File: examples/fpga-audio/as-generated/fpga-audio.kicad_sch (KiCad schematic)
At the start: 29 parts, among them J1 3V3 IN, J2 AUDIO OUT, J3 SPI PROG, U1 iCE40UP5K, U2 PCM5102A, U3 AP2112K-1.2, U4 W25Q32JV, X1 12MHz

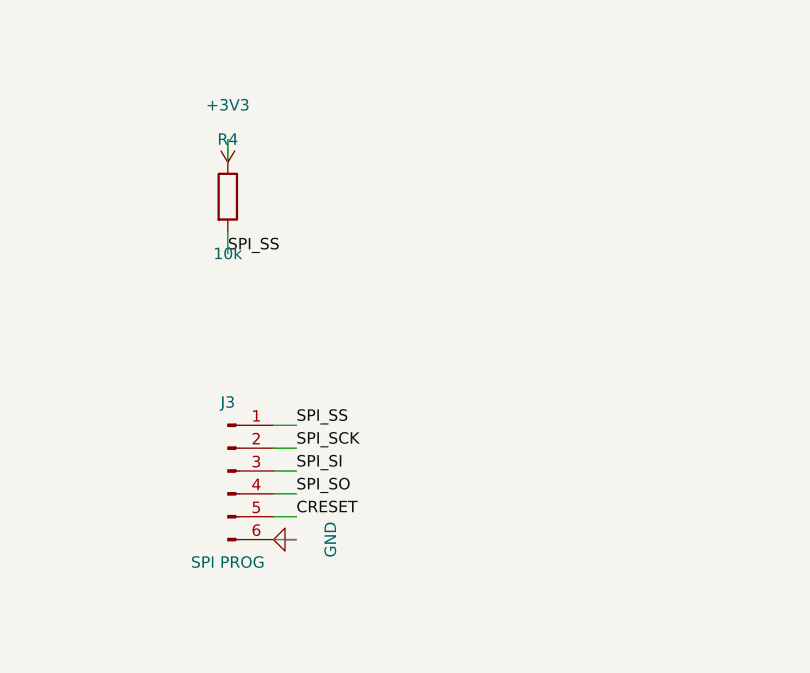
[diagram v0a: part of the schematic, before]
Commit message: Route the sheets, and anchor the ground vias where the loop is
The user's verdict on the last round stood: none of the five schematics
read as a human drawing, and the artwork still had its physics wrong.
This round answers both.

The schematic side replaces the stub-and-label sheet with a router.
Every signal net becomes a tree of straight, L-, Z- and detour-shaped
runs on the 1.27 mm grid: legs leave a pin along its own stub, escape
distances stagger so a bus does not fight over one column, every pin
reserves a runway another wire may cross but not ride along, and the
sheet frame, title block and notes are obstacles like any symbol.
Fragments merge Kruskal-style so a rail whose regulator is boxed in
still gets its capacitors chained; each surviving fragment keeps one
label, because the label is what names the net. Collinear same-net
segments are unioned and then split at every tee - KiCad 9's
connectivity requires files drawn the way the editor draws them, with
a junction dot and a wire break wherever a branch tees in, and a wire
that runs through a junction connects on one side of it only. That
last fact cost an evening and is now a comment.

Trying to draw the wires found what no rule had: the buck's LED was
upside down with its ground pointing up into the resistor above it,
both breakout headers faced away from everything they connect to
(fixed with mirrored symbols, which Part now supports), the FPGA
sheet's notes printed over the 1.2 V regulator, and its programming
header sat inside the title block. Wired: buck, motor and op-amp
completely; the Pico carrier 31 of 33 nets; the FPGA board 16 of 19 -
what stays labelled is what a human would label too.

The artwork side anchors every FPGA decoupling capacitor's ground via
against its own pad, on the far side from the supply pad, with the
1.2 mm stub as the whole loop - retiring all seven
layout.decoupling_via findings and that waiver with them. A back_cost
experiment (0.4 to 0.6) to shrink the return-path cuts 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
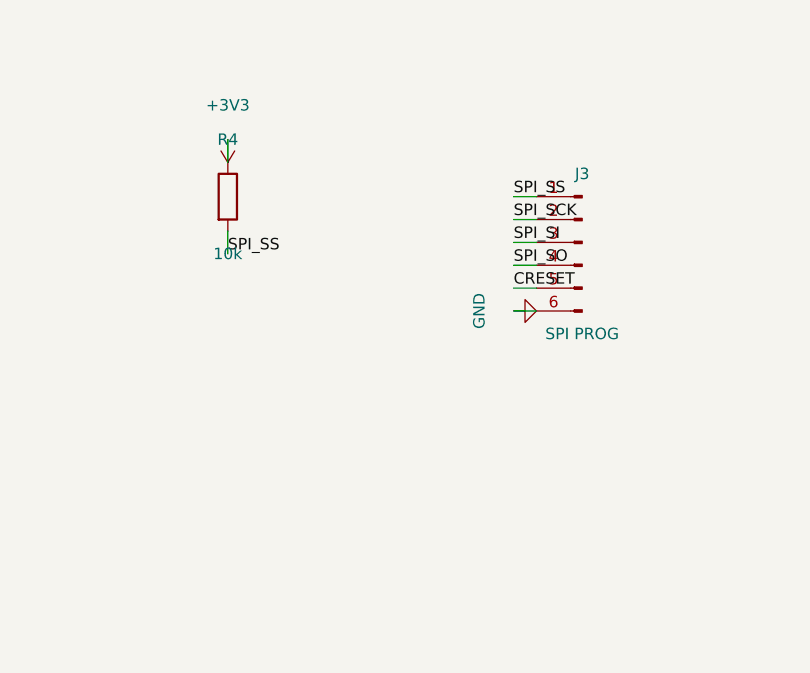
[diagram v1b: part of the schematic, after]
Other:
- moved on the sheet: J3
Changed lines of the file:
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@@
     (instances (project "fpga-audio" (path "/434dea94-d96f-5288-b60c-67317d440f4e" (reference "J2") (unit 1))))
   )
-  (wire (pts (xy 335.59 265.24) (xy 338.13 265.24)) (stroke (width 0) (type default)))
-  (label "SPI_SS" (at 338.13 265.24 0) (effects (font (size 1.27 1.27)) (justify left bottom)))
-  (wire (pts (xy 335.59 267.78) (xy 338.13 267.78)) (stroke (width 0) (type default)))
-  (label "SPI_SCK" (at 338.13 267.78 0) (effects (font (size 1.27 1.27)) (justify left bottom)))
-  (wire (pts (xy 335.59 270.32) (xy 338.13 270.32)) (stroke (width 0) (type default)))
-  (label "SPI_SI" (at 338.13 270.32 0) (effects (font (size 1.27 1.27)) (justify left bottom)))
-  (wire (pts (xy 335.59 272.86) (xy 338.13 272.86)) (stroke (width 0) (type default)))
-  (label "SPI_SO" (at 338.13 272.86 0) (effects (font (size 1.27 1.27)) (justify left bottom)))
-  (wire (pts (xy 335.59 275.4) (xy 338.13 275.4)) (stroke (width 0) (type default)))
-  (label "CRESET" (at 338.13 275.4 0) (effects (font (size 1.27 1.27)) (justify left bottom)))
-  (wire (pts (xy 335.59 277.94) (xy 338.13 277.94)) (stroke (width 0) (type default)))
-  (symbol (lib_id "power:GND") (at 338.13 277.94 270) (unit 1)
+  (wire (pts (xy 364.8 239.84) (xy 362.26 239.84)) (stroke (width 0) (type default)))
+  (label "SPI_SS" (at 362.26 239.84 0) (effects (font (size 1.27 1.27)) (justify left bottom)))
+  (wire (pts (xy 364.8 242.38) (xy 362.26 242.38)) (stroke (width 0) (type default)))
+  (label "SPI_SCK" (at 362.26 242.38 0) (effects (font (size 1.27 1.27)) (justify left bottom)))
+  (wire (pts (xy 364.8 244.92) (xy 362.26 244.92)) (stroke (width 0) (type default)))
+  (label "SPI_SI" (at 362.26 244.92 0) (effects (font (size 1.27 1.27)) (justify left bottom)))
+  (wire (pts (xy 364.8 247.46) (xy 362.26 247.46)) (stroke (width 0) (type default)))
+  (label "SPI_SO" (at 362.26 247.46 0) (effects (font (size 1.27 1.27)) (justify left bottom)))
+  (wire (pts (xy 364.8 250.0) (xy 362.26 250.0)) (stroke (width 0) (type default)))
+  (label "CRESET" (at 362.26 250.0 0) (effects (font (size 1.27 1.27)) (justify left bottom)))
+  (wire (pts (xy 364.8 252.54) (xy 362.26 252.54)) (stroke (width 0) (type default)))
+  (symbol (lib_id "power:GND") (at 362.26 252.54 90) (unit 1)
     (exclude_from_sim no) (in_bom no) (on_board yes) (dnp no)
-    (property "Reference" "#PWR29" (at 338.13 277.94 0) (effects (font (size 1.27 1.27)) hide))
-    (property "Value" "GND" (at 341.94 277.94 0) (effects (font (size 1.27 1.27))))
-    (property "Footprint" "" (at 338.13 277.94 0) (effects (font (size 1.27 1.27)) hide))
-    (property "Datasheet" "" (at 338.13 277.94 0) (effects (font (size 1.27 1.27)) hide))
+    (property "Reference" "#PWR29" (at 362.26 252.54 0) (effects (font (size 1.27 1.27)) hide))
+    (property "Value" "GND" (at 358.45 252.54 0) (effects (font (size 1.27 1.27))))
+    (property "Footprint" "" (at 362.26 252.54 0) (effects (font (size 1.27 1.27)) hide))
+    (property "Datasheet" "" (at 362.26 252.54 0) (effects (font (size 1.27 1.27)) hide))
     (pin "1" (uuid "6e9923b8-75e3-547a-a1bf-3062871e3599-p"))
     (instances (project "fpga-audio" (path "/434dea94-d96f-5288-b60c-67317d440f4e" (reference "#PWR29") (unit 1))))
   )
-  (symbol (lib_id "Connector:Conn_01x06_Pin") (at 330.51 270.32 0.0) (unit 1)
+  (symbol (lib_id "Connector:Conn_01x06_Pin") (at 369.88 244.92 0.0) (mirror y) (unit 1)
     (exclude_from_sim no) (in_bom yes) (on_board yes) (dnp no)
-    (property "Reference" "J3" (at 330.51 262.7 0) (effects (font (size 1.27 1.27))))
-    (property "Value" "SPI PROG" (at 330.51 280.48 0) (effects (font (size 1.27 1.27))))
-    (property "Footprint" "Connector_PinHeader_2.54mm:PinHeader_1x06_P2.54mm_Vertical" (at 330.51 270.32 0) (effects (font (size 1.27 1.27)) hide))
-    (property "Datasheet" "https://www.we-online.com/components/products/datasheet/61300611121.pdf" (at 330.51 270.32 0) (effects (font (size 1.27 1.27)) hide))
+    (property "Reference" "J3" (at 369.88 237.3 0) (effects (font (size 1.27 1.27))))
+    (property "Value" "SPI PROG" (at 369.88 255.08 0) (effects (font (size 1.27 1.27))))
+    (property "Footprint" "Connector_PinHeader_2.54mm:PinHeader_1x06_P2.54mm_Vertical" (at 369.88 244.92 0) (effects (font (size 1.27 1.27)) hide))
+    (property "Datasheet" "https://www.we-online.com/components/products/datasheet/61300611121.pdf" (at 369.88 244.92 0) (effects (font (size 1.27 1.27)) hide))
     (pin "1" (uuid "e626d2b9-eb34-5bd8-9fe1-af5fe30eedde-p1"))
     (pin "2" (uuid "e626d2b9-eb34-5bd8-9fe1-af5fe30eedde-p2"))

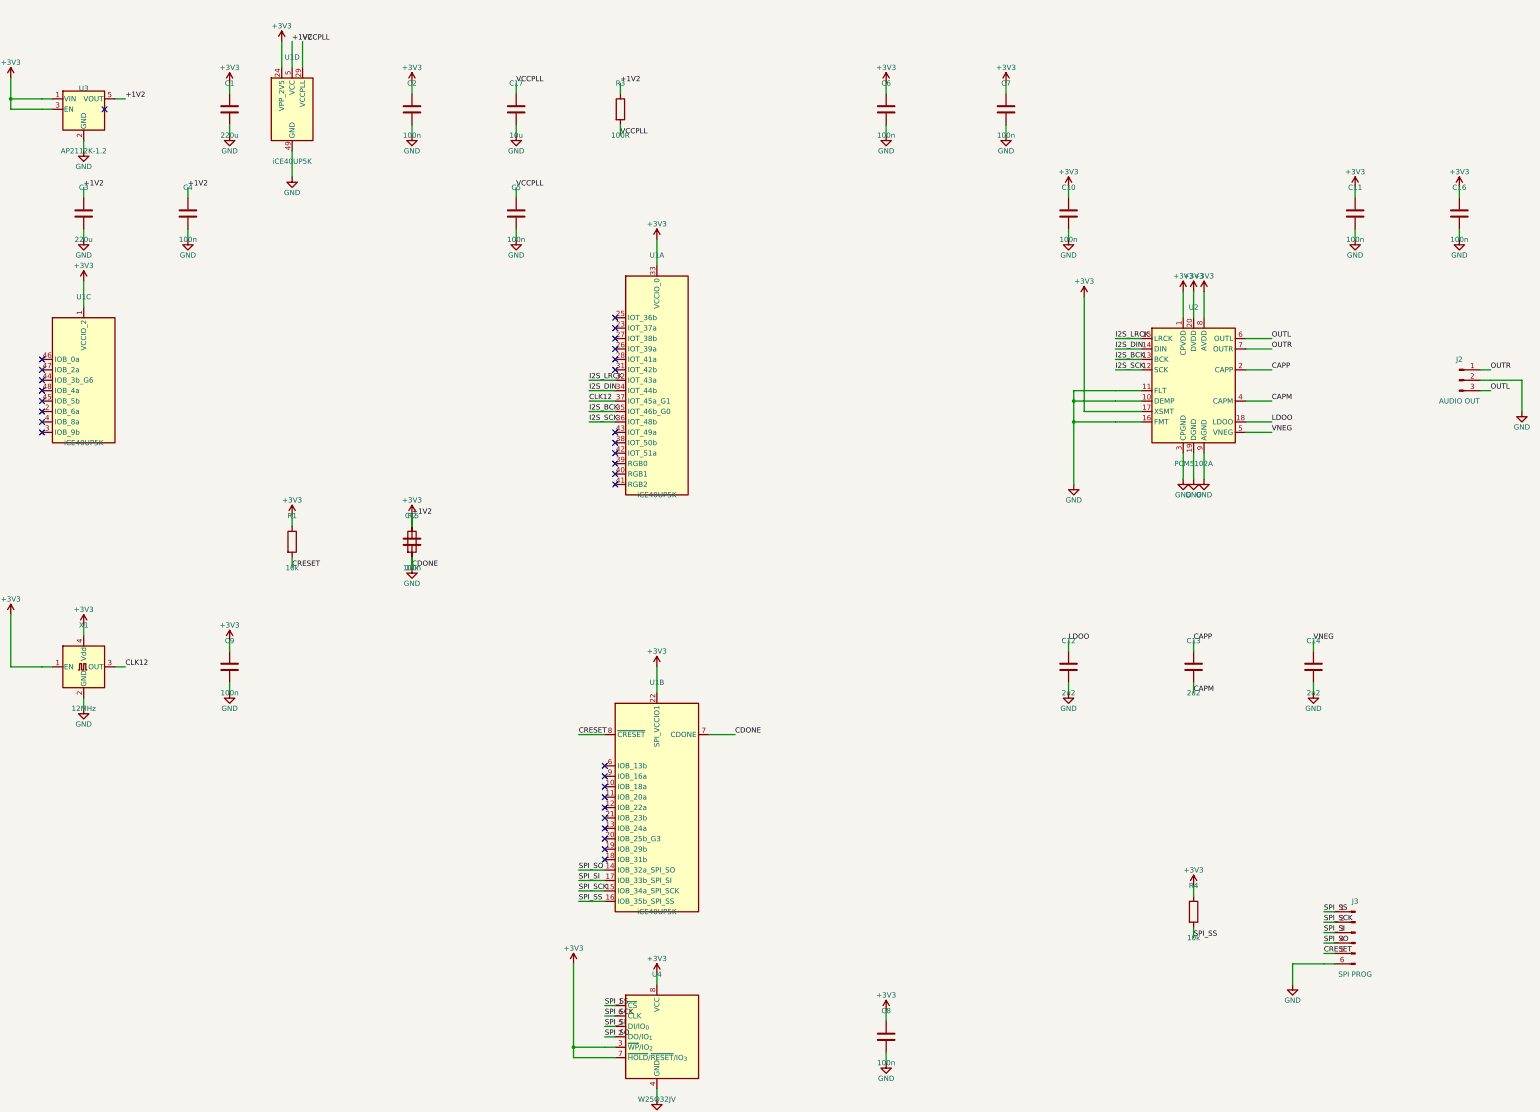
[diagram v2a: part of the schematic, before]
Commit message: Regenerate the five as round three drew them
All five reviewed projects pass their gates again: the buck all wire
with its feedback drawn home, the motor's logic named at the header,
the carrier reading as the pinout table it is - with its feed diode
finally pointing the right way - the filter compact with test points,
and the FPGA's capacitors sitting beside the units they feed. Thirty
renders redrawn, verdict tables at today's numbers.

Co-Authored-By: Claude Fable 5 <noreply@anthropic.com>
Claude-Session: https://claude.ai/code/session_01DUj7Ltu92tWg159mCSacwY
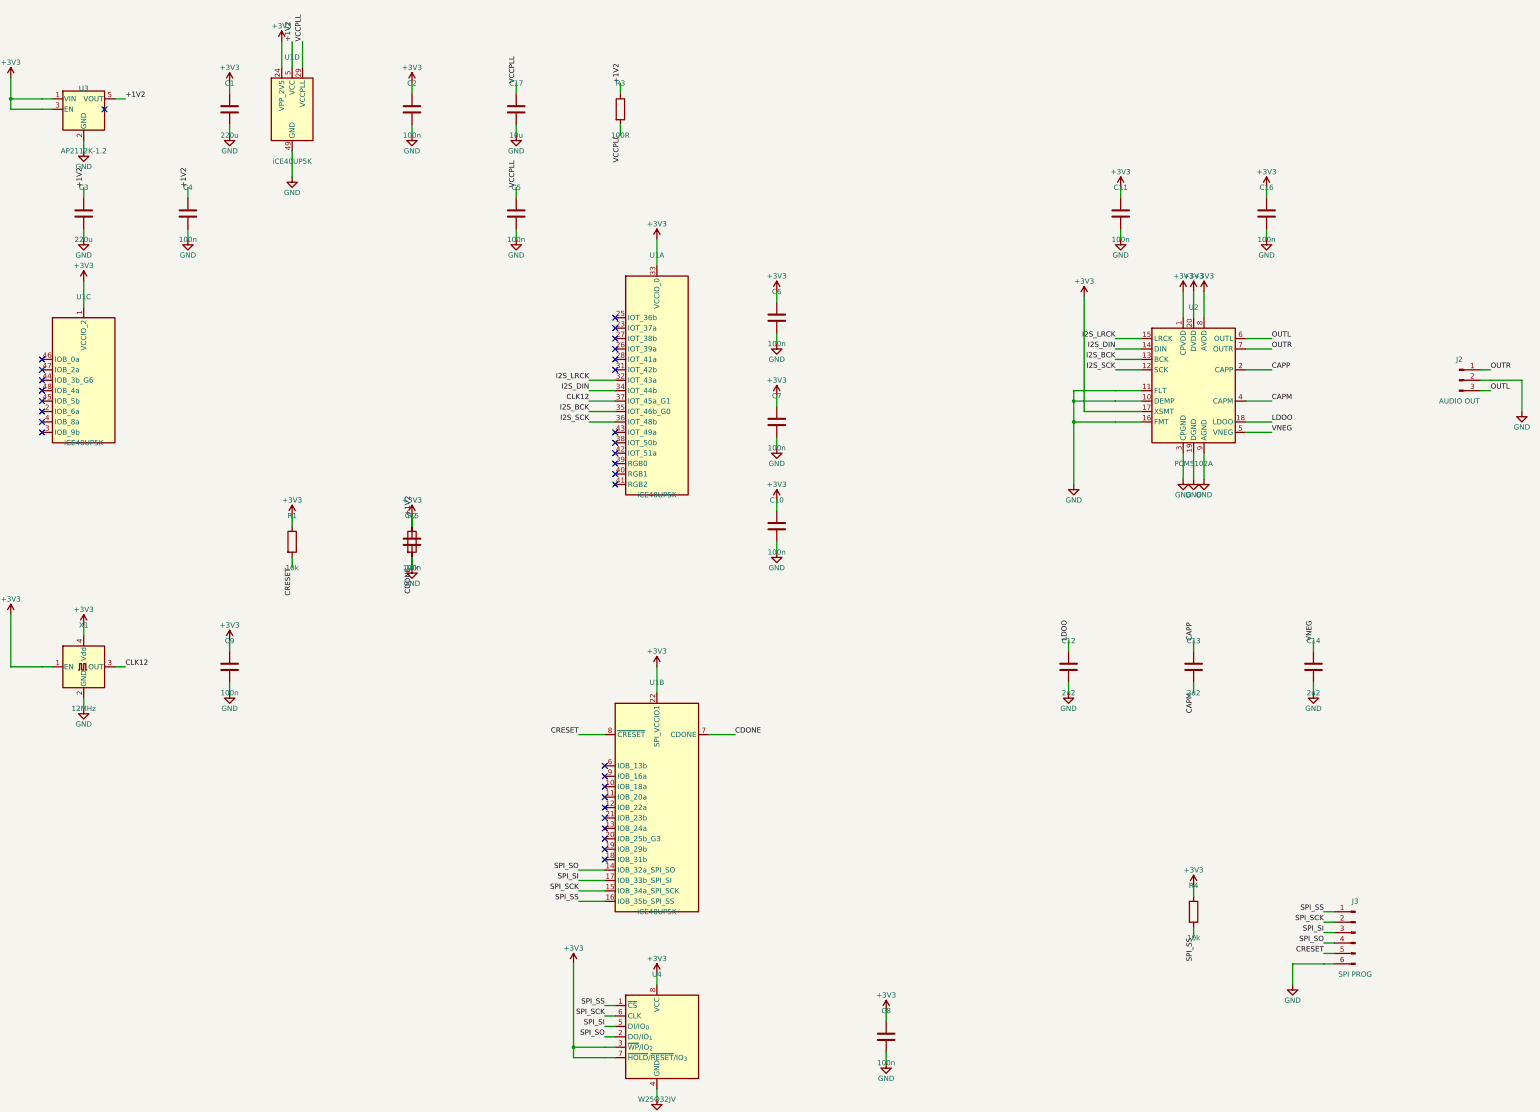
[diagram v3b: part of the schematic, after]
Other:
- moved on the sheet: C10, C11, C16, C6, C7
